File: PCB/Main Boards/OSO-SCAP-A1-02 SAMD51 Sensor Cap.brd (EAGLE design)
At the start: 50.8 x 22.9 mm, 73 parts, among them J1 10118193-0001LF, J2 S2B-PH-SM4-TB(LF)(SN), J3 S3B-PH-SM4-TB(LF)(SN), J4 SM04B-SRSS-TB(LF)(SN), Q1 DMG341, SW1 SPST_TACT-KMR2, SW2 SPST_TACT-KMR2, U1 AP2112-3.3, U2 MCP73831T-2ACI/OT, U3 ATSAMD51G18A-MUT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

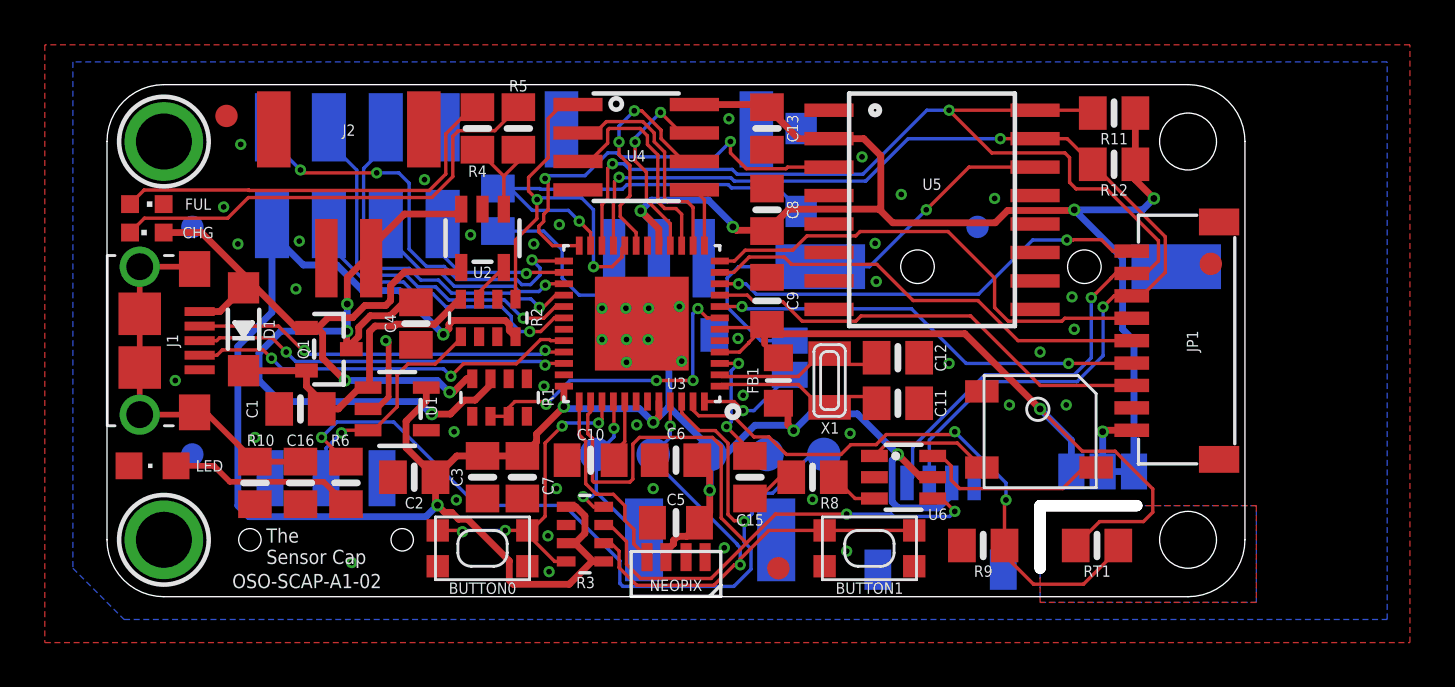
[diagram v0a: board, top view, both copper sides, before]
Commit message: rev 2 of sensor cap
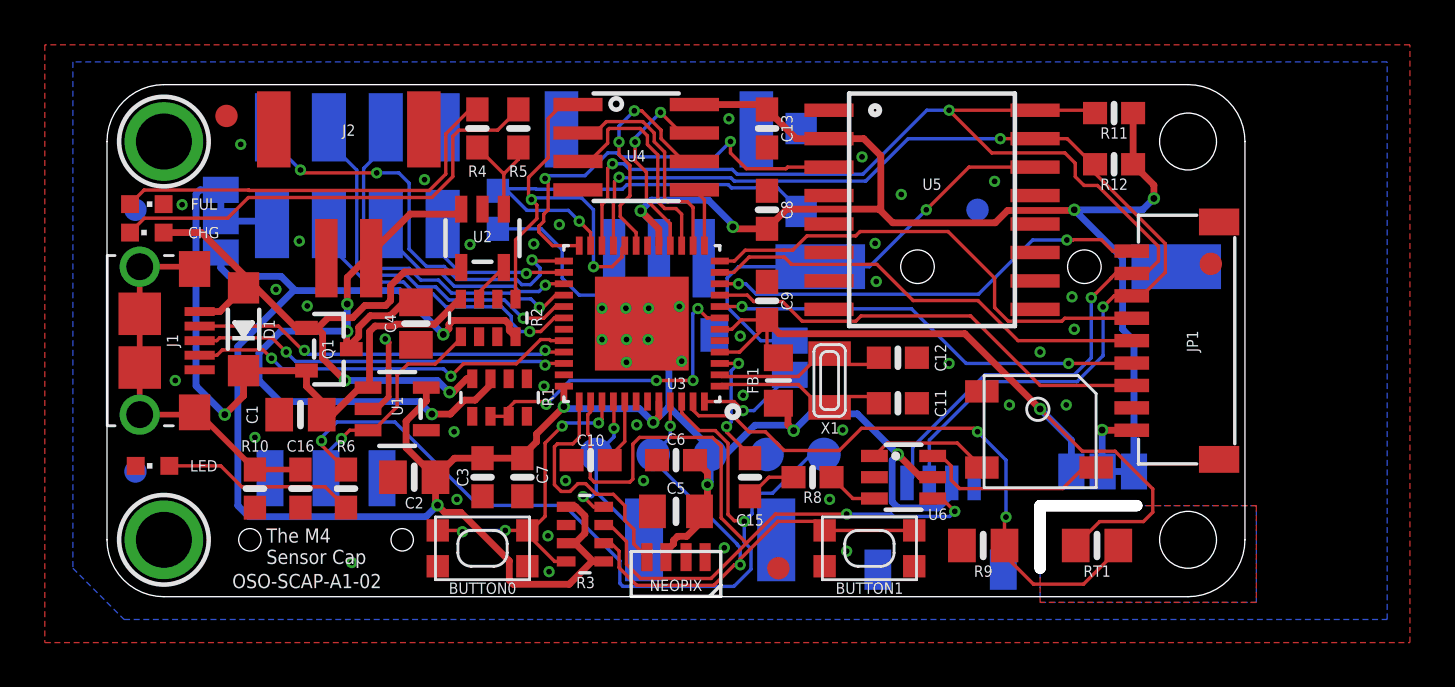
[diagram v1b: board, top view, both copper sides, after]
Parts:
- added SJ3: (no value), pygamer-microbuilder:SOLDERJUMPER_2WAY_OPEN_NOPASTE
- C10, C9: device microbuilder:0805_10MGAP -> microbuilder:0603-NO
- C11, C12, C13, C15, C16, C3, C6, C7, C8, R10, R4, R5, R6, R7, R8: device microbuilder:0805-NO -> microbuilder:0603-NO
- LED: device adafruit:CHIPLED_0805 -> adafruit:CHIPLED_0603
- R11, R12: value 50K -> 10K; device microbuilder:0805-NO -> microbuilder:0603-NO
- moved FID4 2.65 mm to (1.27, 5.59)
- moved FID5 2.65 mm to (1.27, 17.3)
- moved FID6 0.76 mm to (38.9, 17.3)
- moved C5 0.51 mm to (25.4, 3.81)
- moved U$31 0.36 mm to (20.1, 12.2)
- moved C16 0.25 mm to (8.64, 4.83)
- moved R10 0.25 mm to (6.60, 4.83)
- moved R6 0.25 mm to (10.7, 4.83)
- moved C1 0.25 mm to (8.64, 8.13)
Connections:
- new net ACC_POWER: JP2.7, SJ3.2
- net +3V3: now also SJ3.3; no longer JP2.7
- net V+: now also SJ3.1
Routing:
- net V+: track 14.5 -> 28.7 mm, vias 0 -> 1
- net ACC_POWER: track 0.00 -> 4.47 mm
- net NEOPIX: track 8.64 -> 11.1 mm
- net +3V3: track 167.0 -> 164.8 mm
- net POWER_OUT: track 3.10 -> 4.72 mm
- net TS: track 26.2 -> 26.8 mm
- net AVCC: track 35.1 -> 35.6 mm
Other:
- board text added: "SJ1: Power to sensor board. SJ2: Routes coin cell bkup battery to SAMD51 pin 48. SJ3: Power to 2x4 accessory header."
- board text added: "The M4 Sensor Cap"
- board text added: "V+"
- board text removed: "SJ1: Power to sensor board. SJ2: Routes coin cell battery backup to SAMD51 pin 48."
- board text removed: "The Sensor Cap"
